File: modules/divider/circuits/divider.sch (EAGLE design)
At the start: 28 parts

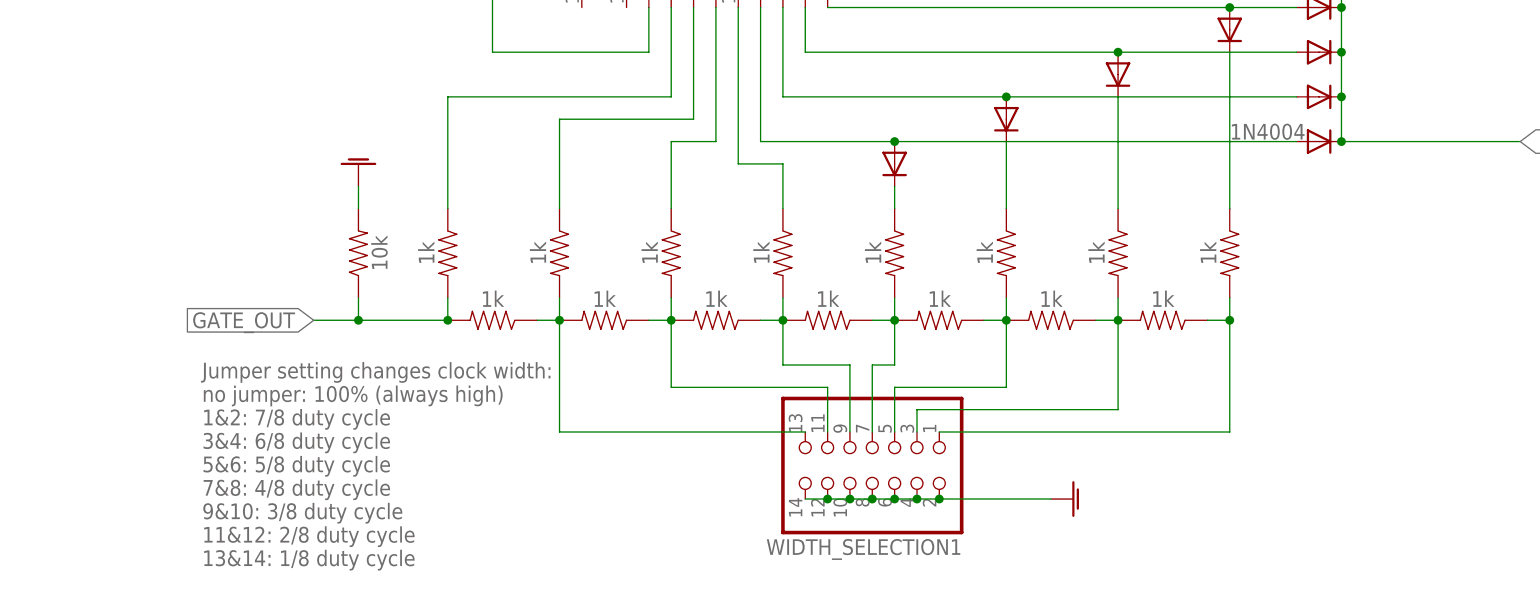
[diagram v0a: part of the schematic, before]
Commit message: adding clock module
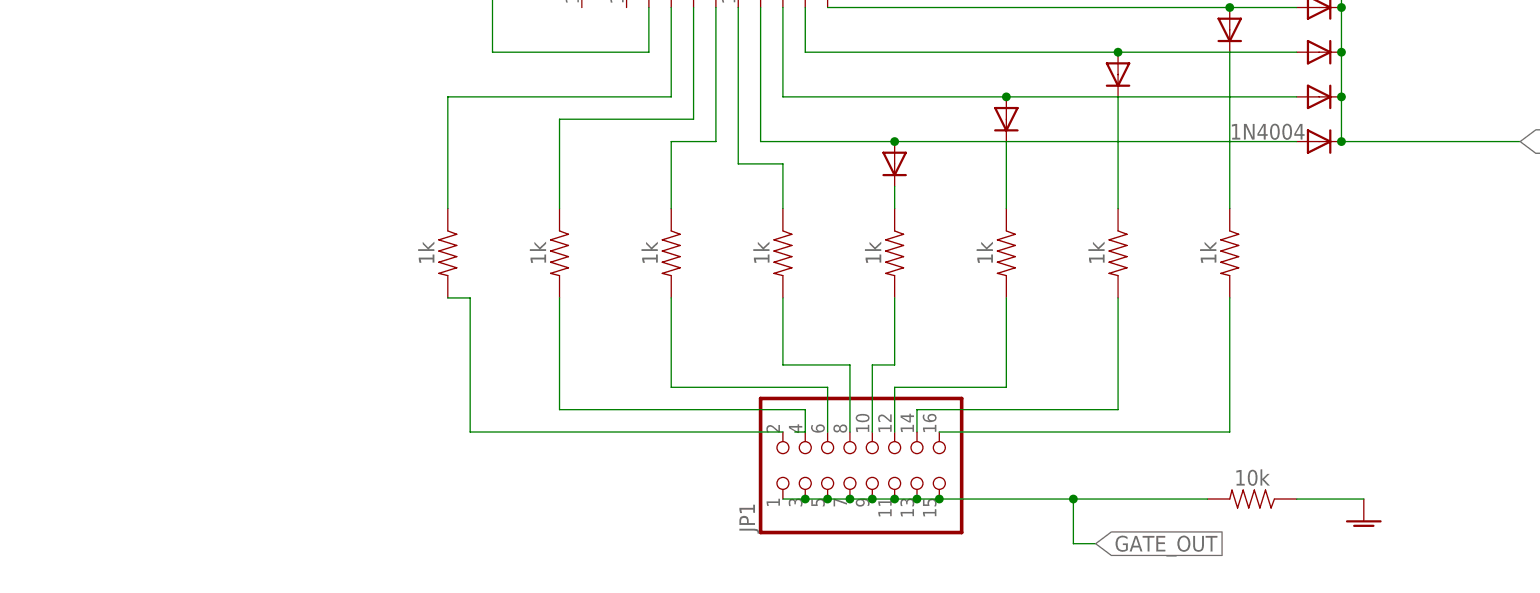
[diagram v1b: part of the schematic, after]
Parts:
- removed R41, R42, R43, R44, R45, R46, R47: 1k, SparkFun-Resistors:10KOHM-HORIZ-1/4W-1%
- removed WIDTH_SELECTION1: (no value), pinhead:PINHD-2X7
- added JP1: (no value), pinhead:PINHD-2X8
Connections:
- removed net N$62: R41.2, R47.1, R49.2, WIDTH_SELECTION1.13
- new net N$1: JP1.4, R49.2
- new net N$2: JP1.2, R48.2
- net GATE_OUT: now also JP1.1, JP1.11, JP1.13, JP1.15, JP1.3, JP1.5, JP1.7, JP1.9, R56.2; no longer R47.2, R48.2, R56.1
- net GNDA: now also R56.1; no longer R56.2, WIDTH_SELECTION1.10, WIDTH_SELECTION1.12, WIDTH_SELECTION1.14, WIDTH_SELECTION1.2, WIDTH_SELECTION1.4, WIDTH_SELECTION1.6, WIDTH_SELECTION1.8
- net N$63: now also JP1.6; no longer R41.1, R42.2, WIDTH_SELECTION1.11
- net N$65: now also JP1.10; no longer R43.1, R44.2, WIDTH_SELECTION1.7
- net N$66: now also JP1.12; no longer R44.1, R45.2, WIDTH_SELECTION1.5
- net N$67: now also JP1.14; no longer R45.1, R46.2, WIDTH_SELECTION1.3
- net N$68: now also JP1.16; no longer R46.1, WIDTH_SELECTION1.1
- net N$71: now also JP1.8; no longer R42.1, R43.2, WIDTH_SELECTION1.9
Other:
- note removed: "Jumper setting changes clock width: no jumper: 100% (always high) 1&2: 7/8 duty cycle 3&4: 6/8 duty cycle 5&6: 5/8 duty cycle 7&8: 4/8 duty cycle 9&10: 3/8 duty cycle 11&12: 2/8 duty cycle 13&14: 1/8 duty cycle"
